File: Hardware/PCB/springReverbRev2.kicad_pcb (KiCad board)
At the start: 2 copper layers, 165 x 174 mm, 92 parts, among them IC102 TL074, IC103 TL074, J1 Conn_01x08, J2 Conn_01x08, J901 AudioJack2_SwitchT, J902 AudioJack2, J903 AudioJack2, J904 AudioJack2, J905 AudioJack2_SwitchT, J906 AudioJack2, SW901 SW_SPDT_MSM, U1 TL072, U2 TL072, U7 NE5532, U901 L78L05_TO92, X101 RCA, X102 RCA

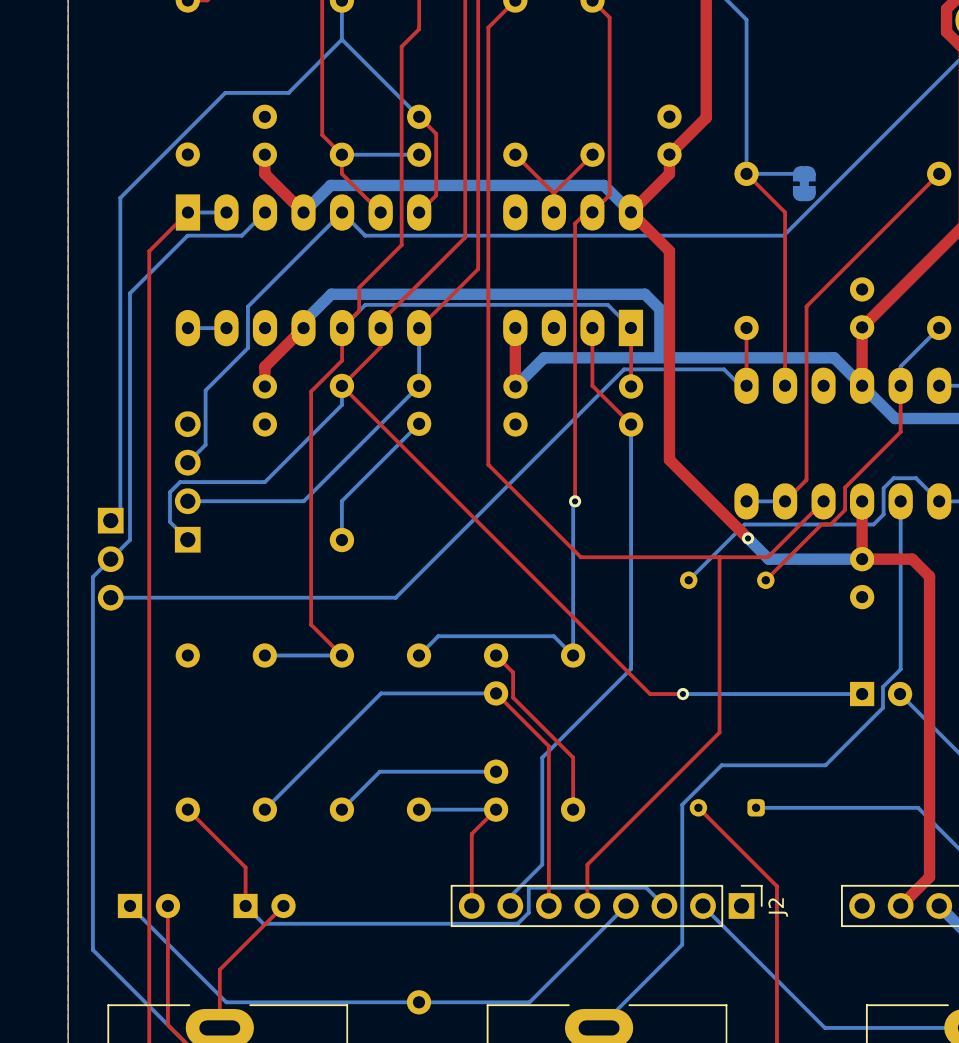
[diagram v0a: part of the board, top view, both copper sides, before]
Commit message: Note on phono jacks, replace pin headers with Molex
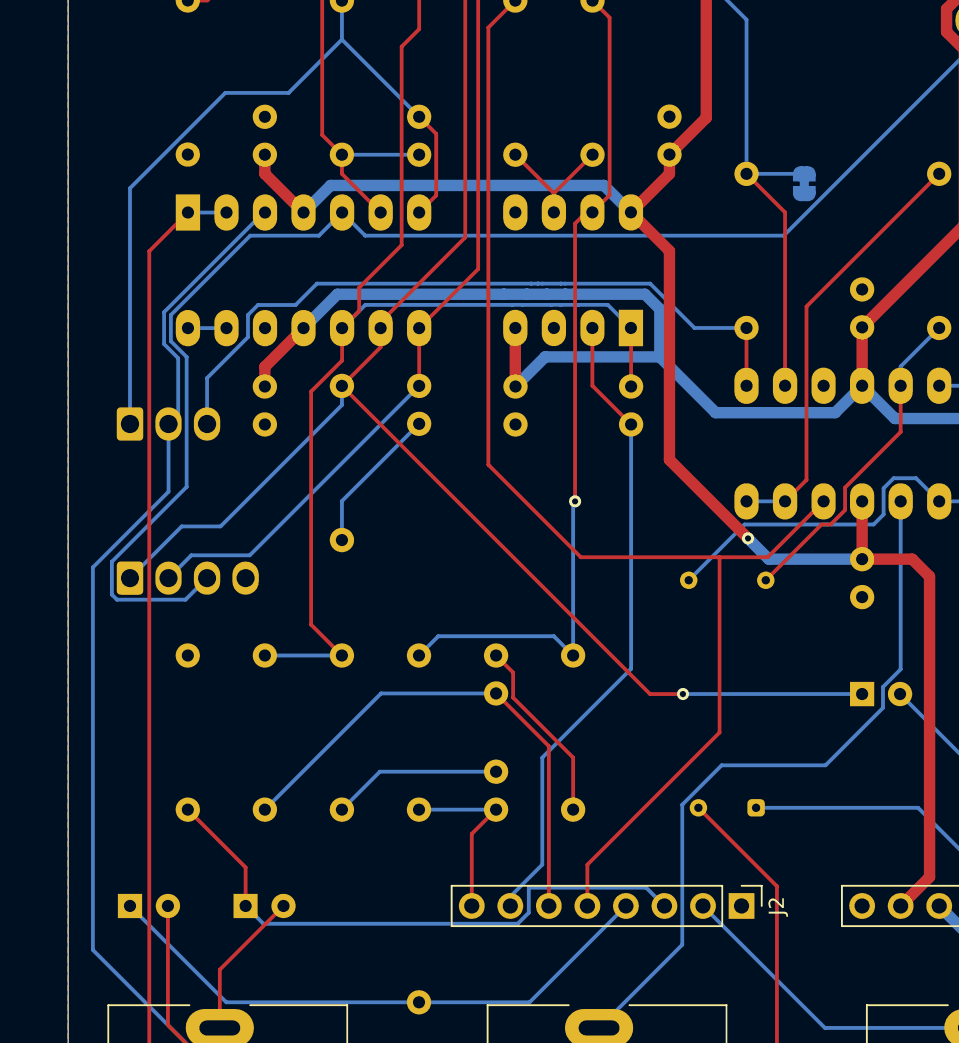
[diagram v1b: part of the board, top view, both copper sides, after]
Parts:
- JP101: footprint Connector_PinHeader_2.54mm:PinHeader_1x04_P2.54mm_Vertical -> Connector_Molex:Molex_KK-254_AE-6410-04A_1x04_P2.54mm_Vertical
- JP102: footprint Connector_PinHeader_2.54mm:PinHeader_1x03_P2.54mm_Vertical -> ao_tht:Molex_KK-254_AE-6410-03A_1x03_P2.54mm_Vertical
- moved JP102 6.50 mm to (168.6, 103.8), turned to 0 degrees
- moved JP101 4.57 mm to (168.6, 114.0)
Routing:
- net /Back board/FROM_TANK: track 81.1 -> 102.4 mm
- net Net-(C110-Pad2): track 57.5 -> 50.6 mm
- net Net-(IC103-Pad8): track 52.4 -> 47.1 mm
- net Net-(C108-Pad1): track 93.4 -> 96.7 mm
- net /Back board/TO_TANK: track 137.0 -> 138.3 mm
- net -12V_B: track 210.1 -> 211.4 mm
- net /Back board/REVERB_RETURN: track 86.6 -> 85.3 mm

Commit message: Layout redone
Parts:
- added H901: MountingHole, ao_tht:MountingHole_3.2mm_M3, F.Cu at (173.5, 31.5)
- added H902: MountingHole, ao_tht:MountingHole_3.2mm_M3, F.Cu at (232.5, 31.5)
- added H903: MountingHole, ao_tht:MountingHole_3.2mm_M3, F.Cu at (73.5, 31.5)
- added H904: MountingHole, ao_tht:MountingHole_3.2mm_M3, F.Cu at (132.5, 31.5)
- added TP904: +12V, ao_tht:TestPoint_THTPad_D1.5mm_Drill0.7mm, F.Cu at (133.0, 116.5)
- added TP905: GND, ao_tht:TestPoint_THTPad_D1.5mm_Drill0.7mm, F.Cu at (133.0, 124.1)
- added TP906: -12V, ao_tht:TestPoint_THTPad_D1.5mm_Drill0.7mm, F.Cu at (133.0, 130.5)
- C1, C101, C102, C103, C104, C105, C106, C107, C109, C2, C6, C7, C901, C902, C903, C904, D901, D902, IC102, IC103, R1, R10, R101, R102, R103, R104, R105, R106, R107, R108, R109, R11, R110, R12, R13, R16, R18, R19, R2, R20, R21, R22, R23, R24, R25, R26, R3, R6, R7, R8, R9, R901, R902, U1, U2, U7, U901, V101: moved to F.Cu
- C108, C110, C3, C4: footprint ao_tht:C_Disc_D3.0mm_W1.6mm_P2.50mm -> ao_tht:C_Rect_L7.2mm_W2.5mm_P5.00mm_FKS2_FKP2_MKS2_MKP2; moved to F.Cu
- C5: footprint ao_tht:C_Disc_D3.0mm_W1.6mm_P2.50mm -> ao_tht:C_Disc_D5.0mm_W2.5mm_P5.00mm; moved to F.Cu
- X101, X102: footprint ao_tht:Jack_6.35mm_PJ_629HAN_slots -> springreverb:RCJ-02
- moved R8 78.7 mm to (124.1, 55.5), turned to 180 degrees
- moved JP102 69.9 mm to (229.6, 69.5), turned to -90 degrees
- moved JP101 68.7 mm to (229.6, 82.2), turned to -90 degrees
- moved X101 57.2 mm to (228.3, 108.9)
- moved IC103 56.0 mm to (194.0, 61.9), turned to 0 degrees
- moved X102 55.9 mm to (228.3, 126.7)
- moved C4 54.3 mm to (222.0, 83.5), turned to 180 degrees
- moved C902 52.1 mm to (187.6, 69.5), turned to 180 degrees
- moved V101 50.6 mm to (172.6, 94.8)
- moved R110 50.0 mm to (177.5, 74.6), turned to 0 degrees
- moved R9 46.6 mm to (114.0, 60.6), turned to 0 degrees
- moved R106 45.5 mm to (187.6, 110.2), turned to 180 degrees
- moved R11 45.5 mm to (208.0, 78.4), turned to 0 degrees
- moved R107 43.4 mm to (187.6, 35.2), turned to 180 degrees
- moved R19 41.1 mm to (218.1, 122.9), turned to 180 degrees
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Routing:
- net /Front board/AUDIO_IN_1: track 5.61 -> 110.1 mm
- net /Back board/VAC_CA_B: track 19.8 -> 101.5 mm
- net /Back board/EQ_POT_1_B: track 12.1 -> 92.7 mm, vias 0 -> 1
- net /Back board/TO_TANK: track 138.3 -> 58.7 mm, vias 2 -> 1
- net Net-(LED1-Pad1): track 28.1 -> 95.8 mm, vias 0 -> 1
- net Net-(C109-Pad2): track 25.7 -> 88.0 mm
- net -12V_B: track 211.4 -> 157.8 mm, vias 0 -> 1
- net Net-(C110-Pad2): track 50.6 -> 103.5 mm
- net /Back board/MIX: track 77.1 -> 119.3 mm
- net /Front board/FB_ON: track 17.0 -> 56.6 mm
- net /Back board/EQ_POT_3_B: track 33.9 -> 73.3 mm, vias 0 -> 1
- net /Back board/XFADE: track 47.0 -> 86.2 mm, vias 0 -> 1
- net Net-(C108-Pad1): track 96.7 -> 58.8 mm, vias 1 -> 0
- net Net-(C4-Pad2): track 11.2 -> 47.3 mm
- net Net-(R8-Pad2): track 62.0 -> 26.9 mm
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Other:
- board size 165 x 174 mm -> 165 x 159.5 mm

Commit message: phono jacks
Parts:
- V101: footprint OptoDevice:PerkinElmer_VTL5C -> ao_tht:Vactrol_VTL5C
- X101: footprint springreverb:RCJ-02 -> springreverb:RCJ-023 white
- X102: footprint springreverb:RCJ-02 -> springreverb:RCJ-022 red
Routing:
- net Net-(LED1-Pad1): track 95.8 -> 97.4 mm
- net Net-(IC103-Pad12): track 34.9 -> 36.1 mm
- net Net-(IC103-Pad1): track 30.2 -> 31.1 mm
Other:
- board text added: "RED = FROM"
- board text added: "WHITE = TO"
